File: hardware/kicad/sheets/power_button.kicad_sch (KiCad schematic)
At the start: 23 parts, among them J7 PANEL BUTTON, Q1 IRF4905S, Q2 BSS138, Q3 BSS138, Q4 BSS138, SW3 POWER, U11 LTC2954CTS8-2, U12 LM4040DBZ-5, U13 CL25N8-G

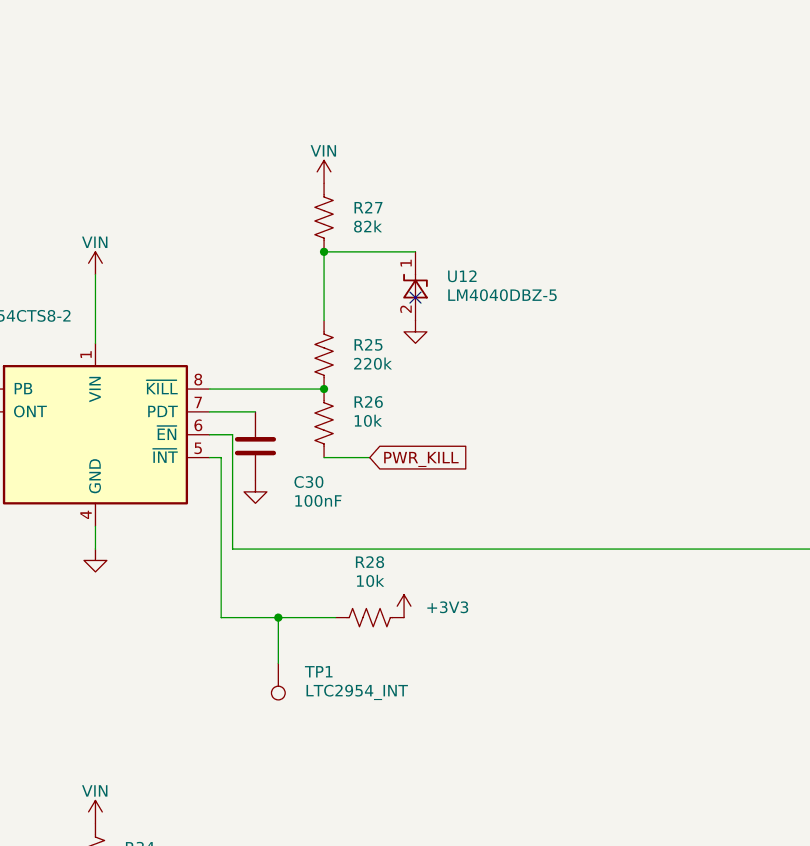
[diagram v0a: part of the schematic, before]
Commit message: WIP: restructure PCB for the Phoenix UCS 125-87 housing
Work in progress, layout not finished: about 90 parts still do not fit
their sections and the board is not routed.

- Right-angle connectors: Phoenix MSTBA 2,5 / MC 1,5, JST XH side entry,
  Hirose DF13, Molex 505448-0871 (new footprint from the Molex drawing)
- Datasheet and product links on every symbol (tools/part_links.py)
- Test points so every IC has one on its own nets
- gen_pcb.py: 100 x 62 mm two-sided board, housing holes and restricted
  corners, ESP32 antenna notch, one section per sheet, board ID block,
  ESP32 pin names, pin-1 marks, blue mask
- Housing drawings in hardware/housing/

Co-Authored-By: Claude Opus 5.5 <noreply@anthropic.com>
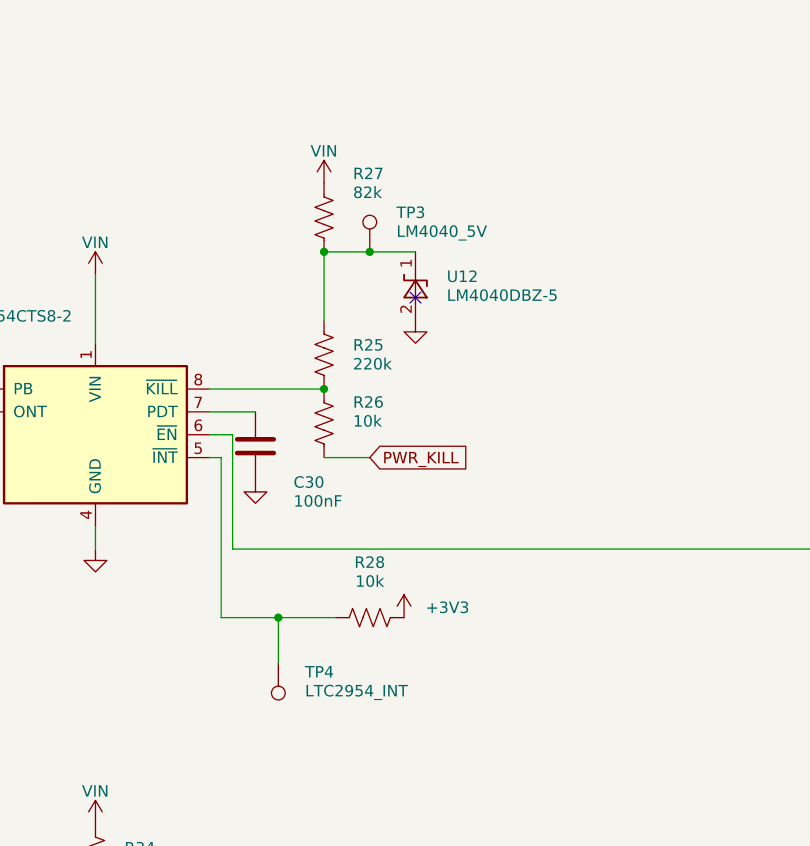
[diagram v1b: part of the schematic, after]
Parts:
- removed C29: 100nF, Capacitor_SMD:C_0603_1608Metric, symbol Device:C
- removed D3: RED/GREEN, LED_SMD:LED_1206_3216Metric, symbol Device:LED_Dual_Bidirectional
- removed R30: 330, Resistor_SMD:R_0603_1608Metric, symbol Device:R_US
- removed TP1: LTC2954_INT, TestPoint:TestPoint_Pad_D1.5mm, symbol Connector:TestPoint
- removed U13: CL25N8-G, Package_TO_SOT_SMD:SOT-89-3, symbol cryocooler:CL25N8-G
- added C30: 100nF, Capacitor_SMD:C_0603_1608Metric, symbol Device:C
- added Q1: IRF4905S, Package_TO_SOT_SMD:TO-263-3_TabPin2, symbol Transistor_FET:IRF4905
- added Q2, Q3: BSS138, Package_TO_SOT_SMD:SOT-23, symbol Transistor_FET:BSS138
- added R31: 330, Resistor_SMD:R_0603_1608Metric, symbol Device:R_US
- added TP4: LTC2954_INT, TestPoint:TestPoint_Pad_D1.5mm, symbol Connector:TestPoint
- C29: renamed from SW3; value POWER -> 100nF; footprint Button_Switch_SMD:SW_SPST_TL3342 -> Capacitor_SMD:C_0603_1608Metric; symbol Switch:SW_Push -> Device:C; Product (none) -> https://www.digikey.com/en/products/result?keywords=C0603C1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
- D3: renamed from Q3; value BSS138 -> RED/GREEN; footprint Package_TO_SOT_SMD:SOT-23 -> LED_SMD:LED_1206_3216Metric; symbol Transistor_FET:BSS138 -> Device:LED_Dual_Bidirectional; Product (none) -> https://www.digikey.com/en/products/result?keywords=XZMDKVG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
- J7: renamed from R25; value 220k -> PANEL BUTTON; footprint Resistor_SMD:R_0603_1608Metric -> Connector_Hirose:Hirose_DF13-02P-1.25DS_1x02_P1.25mm_Horizontal; symbol Device:R_US -> Connector_Generic:Conn_01x02; Product (none) -> https://www.digikey.com/en/products/result?keywords=DF13-2P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
- Q4: Product (none) -> https://www.digikey.com/en/products/result?keywords=BSS138-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
- R25: renamed from R27; value 82k -> 220k; Product (none) -> https://www.digikey.com/en/products/result?keywords=RC0603F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
- R26, R29, R32, R33, R34: Product (none) -> https://www.digikey.com/en/products/result?keywords=AR0603F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
- R27: renamed from U12; value LM4040DBZ-5 -> 82k; footprint Package_TO_SOT_SMD:SOT-23 -> Resistor_SMD:R_0603_1608Metric; symbol Reference_Voltage:LM4040DBZ-5 -> Device:R_US; Product (none) -> https://www.digikey.com/en/products/result?keywords=RC0603F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
- R28: renamed from Q1; value IRF4905S -> 10k; footprint Package_TO_SOT_SMD:TO-263-3_TabPin2 -> Resistor_SMD:R_0603_1608Metric; symbol Transistor_FET:IRF4905 -> Device:R_US; Product (none) -> https://www.digikey.com/en/products/result?keywords=AR0603F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
- R30: renamed from Q2; value BSS138 -> 330; footprint Package_TO_SOT_SMD:SOT-23 -> Resistor_SMD:R_0603_1608Metric; symbol Transistor_FET:BSS138 -> Device:R_US; Product (none) -> https://www.digikey.com/en/products/result?keywords=RC0603F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
- SW3: renamed from J7; value PANEL BUTTON -> POWER; footprint Connector_JST:JST_XH_B2B-XH-A_1x02_P2.50mm_Vertical -> Button_Switch_SMD:SW_SPST_TL3342; symbol Connector_Generic:Conn_01x02 -> Switch:SW_Push; Product (none) -> https://www.digikey.com/en/products/result?keywords=TL3342F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
- TP3: renamed from R28; value 10k -> LM4040_5V; footprint Resistor_SMD:R_0603_1608Metric -> TestPoint:TestPoint_Pad_D1.5mm; symbol Device:R_US -> Connector:TestPoint
- U11: Product (none) -> https://www.digikey.com/en/products/result?keywords=LTC2954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
- U12: renamed from C30; value 100nF -> LM4040DBZ-5; footprint Capacitor_SMD:C_0603_1608Metric -> Package_TO_SOT_SMD:SOT-23; symbol Device:C -> Reference_Voltage:LM4040DBZ-5; Product (none) -> https://www.digikey.com/en/products/result?keywords=LM4040D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
- U13: renamed from R31; value 330 -> CL25N8-G; footprint Resistor_SMD:R_0603_1608Metric -> Package_TO_SOT_SMD:SOT-89-3; symbol Device:R_US -> cryocooler:CL25N8-G; Product (none) -> https://www.digikey.com/en/products/result?keywords=CL25N8-G
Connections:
- net +3V3: now also R28.2; no longer TP3.2
- net GND: now also J7.2 (Pin_2), C30.2, Q2.2 (S), Q3.2 (S); no longer D3.2 (S), R27.2 (A), R30.2 (S)
- net VIN: now also C29.1, R27.1, U13.1 (VA), Q1.3 (S); no longer R25.1, R28.3 (S)
- net VSW: now also Q1.2 (D); no longer R28.2 (D)
- net at SW3.1, U11.2 (PB): now also J7.1 (Pin_1); no longer C29.1
- net at R29.2, U11.6 (~{EN}): now also Q1.1 (G); no longer R28.1 (G)
- net at U11.5 (~{INT}): now also R28.1, TP4.1; no longer TP3.1
- net at Q4.1 (G), R32.2, R33.1: now also Q2.1 (G); no longer R30.1 (G)
- net at U11.7 (PDT): now also C30.1; no longer U12.1
- net at R26.1, U11.8 (~{KILL}): now also R25.2; no longer J7.2
- net at Q4.3 (D), R34.2: now also Q3.1 (G); no longer D3.1 (G)
- net at U13.2 (VB): now also R30.1, R31.1; no longer D3.3 (D)
- new net: D3.2 (AK), Q2.3 (D), R30.2
- new net: D3.1 (KA), Q3.3 (D), R31.2
- new net: R25.1, R27.2, TP3.1, U12.1 (K)
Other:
- moved on the sheet: R25, R27

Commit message: Lay out the board for the Phoenix UCS 145-125 housing
Move to a 120 x 100 mm, 4-layer, blue-mask board for the UCS 145-125-F-CCD
7035 housing: housing mounting holes and restricted corners, ESP32 antenna
over a routed notch, one labelled section per schematic sheet with almost
every part on top. Placed, routed and cleaned up: DRC 0 errors, 0
unconnected, 0 schematic-parity issues; ERC 0; 193/193 datasheet rules.

- AGENTS.md: test points go on the same side as the part they test, close
  to it
- gen_pcb: test points held to their IC's side and within 8 mm; silkscreen
  check measures text by ink and also fails on pads, part outlines, section
  lines and pin-1 dots; titles along or up a border; connector labels and
  ESP32 pin names reserved before the passives; pin-1 dots only where the
  footprint has no mark; footprints carry the schematic's library links and
  fields; mounting holes are board-only H1-H4
- fix_route: generic clean-up (no old-board coordinate edits); removes GND
  vias in keep-outs or on foreign pads, links stranded ground pads, nudges
  squeezed tracks, handles back-side pour islands
- kicad_dru: fix the rule file (an invalid USB-C rule made KiCad ignore it);
  housing-corner and antenna keep-out part rules
- schematic: pad test points excluded from the BOM
- README / fabrication README updated for the new board

Co-Authored-By: Claude Opus 5.5 <noreply@anthropic.com>
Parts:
- TP3, TP4: now left out of the parts list
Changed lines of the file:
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@@
 		(body_style 1)
 		(exclude_from_sim no)
-		(in_bom yes)
+		(in_bom no)
 		(on_board yes)
 		(in_pos_files yes)
@@
 		(body_style 1)
 		(exclude_from_sim no)
-		(in_bom yes)
+		(in_bom no)
 		(on_board yes)
 		(in_pos_files yes)

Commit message: Use an M12 receptacle for the PT1000 and JST PH headers for the 2-pin I/O
- J10 (cold head PT1000): TE T4145035041-001, M12 A-coded 4-pin female,
  right angle, shielded, panel and PCB mount through the right side wall;
  footprint from TE drawing T41450350X1001 rev B
- J6, J7, J13 (NTC, panel button, relay out): Adafruit 1769 (4UCON 17311),
  JST PH compatible 2-pin right-angle SMT; footprint from its drawing
- BOM, part links and 3D envelopes for both; schematic nets unchanged
- gen_pcb: ground fan-out before routing (a locked via and short track per
  small ground pad, clear of other holes) so no ground pad is left on a
  pour island; fallback labels must sit inside a section box
- fix_route: skip paste apertures (not non-plated holes) as foreign copper,
  nudge tracks off crowded pads, remove GND vias that crowd another hole

DRC 0 errors, 0 unconnected, 0 schematic-parity issues; ERC 0; 193/193
datasheet rules.

Co-Authored-By: Claude Opus 5.5 <noreply@anthropic.com>
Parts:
- J7: footprint Connector_Hirose:Hirose_DF13-02P-1.25DS_1x02_P1.25mm_Horizontal -> cryocooler:Adafruit_1769_JST-PH_1x02_P2.00mm_Horizontal_SMD; Product https://www.digikey.com/en/products/result?keywords=DF13-2P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 -> https://www.adafruit.com/product/1769
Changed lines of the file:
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@@
 			)
 		)
-		(property "Footprint" "Connector_Hirose:Hirose_DF13-02P-1.25DS_1x02_P1.25mm_Horizontal"
+		(property "Footprint" "cryocooler:Adafruit_1769_JST-PH_1x02_P2.00mm_Horizontal_SMD"
 			(at 30.48 83.82 0)
 			(hide yes)
@@
 			)
 		)
-		(property "Datasheet" "https://www.hirose.com/api/v1/series/DF13/documents/product_series_catalog/content?lang=EN"
+		(property "Datasheet" "https://cdn-shop.adafruit.com/datasheets/17311.pdf"
 			(at 30.48 83.82 0)
 			(hide yes)
@@
 			)
 		)
-		(property "Product" "https://www.digikey.com/en/products/result?keywords=DF13-2P-1.25DS%2825%29"
+		(property "Product" "https://www.adafruit.com/product/1769"
 			(at 30.48 83.82 0)
 			(hide yes)
